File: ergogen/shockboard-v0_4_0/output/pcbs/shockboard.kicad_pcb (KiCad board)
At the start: 2 copper layers, 282.9 x 126 mm, 169 parts

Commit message: feat: added mounting holes
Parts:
- moved _8 12.2 mm to (316.2, 136.9)
- moved _7 12.2 mm to (108.6, 136.9)
- moved _3 11.1 mm to (97.5, 93.2)
- moved _4 11.1 mm to (327.3, 93.2)
- moved _1 11.1 mm to (173.7, 96.8)
- moved _2 11.1 mm to (251.0, 96.8)
- moved _6 10.6 mm to (258.8, 152.3)
- moved _5 10.6 mm to (165.9, 152.3)
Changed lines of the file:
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@@
     )
     (module "MountingHole_2.2mm_M2_Pad_Via" (version 20210722) (generator pcbnew) (layer "F.Cu")
-      (at 183.9168487 92.4964472 -8)
+      (at 173.7160154 96.8188307 -8)
       (fp_text reference "_1" (at 0 -3.2) (layer "F.SilkS") hide
         (effects (font (size 1 1) (thickness 0.15)))
@@
     )
     (module "MountingHole_2.2mm_M2_Pad_Via" (version 20210722) (generator pcbnew) (layer "F.Cu")
-      (at 240.83969309999998 92.4964472 8)
+      (at 251.04052639999998 96.8188307 8)
       (fp_text reference "_2" (at 0 -3.2) (layer "F.SilkS") hide
         (effects (font (size 1 1) (thickness 0.15)))
@@
     )
     (module "MountingHole_2.2mm_M2_Pad_Via" (version 20210722) (generator pcbnew) (layer "F.Cu")
-      (at 88.8671705 86.2068791 -8)
+      (at 97.4814305 93.1735516 -8)
       (fp_text reference "_3" (at 0 -3.2) (layer "F.SilkS") hide
         (effects (font (size 1 1) (thickness 0.15)))
@@
     )
     (module "MountingHole_2.2mm_M2_Pad_Via" (version 20210722) (generator pcbnew) (layer "F.Cu")
-      (at 335.8893713 86.2068791 8)
+      (at 327.2751113 93.1735516 8)
       (fp_text reference "_4" (at 0 -3.2) (layer "F.SilkS") hide
         (effects (font (size 1 1) (thickness 0.15)))
@@
     )
     (module "MountingHole_2.2mm_M2_Pad_Via" (version 20210722) (generator pcbnew) (layer "F.Cu")
-      (at 175.983982 148.9417271 -8)
+      (at 165.9153631 152.32335600000002 -8)
       (fp_text reference "_5" (at 0 -3.2) (layer "F.SilkS") hide
         (effects (font (size 1 1) (thickness 0.15)))
@@
     )
     (module "MountingHole_2.2mm_M2_Pad_Via" (version 20210722) (generator pcbnew) (layer "F.Cu")
-      (at 248.77255979999998 148.9417271 8)
+      (at 258.8411787 152.32335600000002 8)
       (fp_text reference "_6" (at 0 -3.2) (layer "F.SilkS") hide
         (effects (font (size 1 1) (thickness 0.15)))
@@
     )
     (module "MountingHole_2.2mm_M2_Pad_Via" (version 20210722) (generator pcbnew) (layer "F.Cu")
-      (at 99.7493971 145.296448 -8)
+      (at 108.5975789 136.9466169 -8)
       (fp_text reference "_7" (at 0 -3.2) (layer "F.SilkS") hide
         (effects (font (size 1 1) (thickness 0.15)))
@@
     )
     (module "MountingHole_2.2mm_M2_Pad_Via" (version 20210722) (generator pcbnew) (layer "F.Cu")
-      (at 325.00714469999997 145.296448 8)
+      (at 316.15896289999995 136.9466169 8)
       (fp_text reference "_8" (at 0 -3.2) (layer "F.SilkS") hide
         (effects (font (size 1 1) (thickness 0.15)))

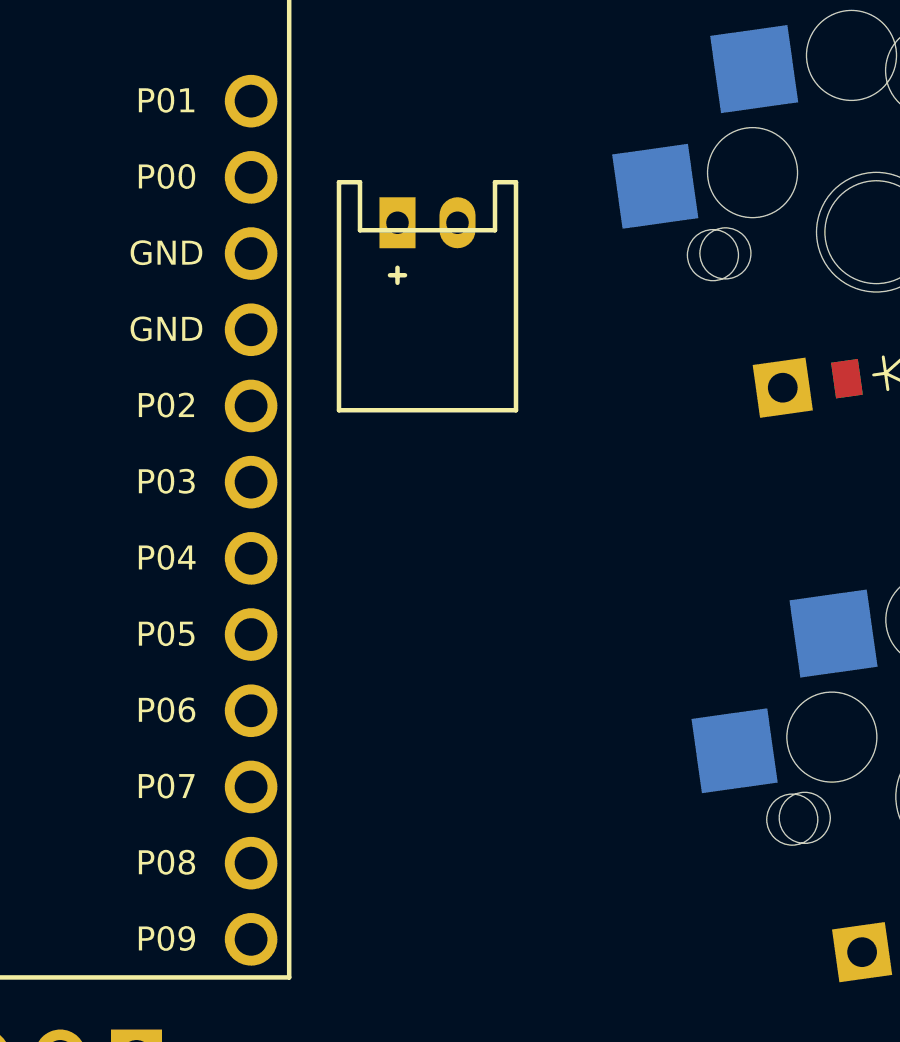
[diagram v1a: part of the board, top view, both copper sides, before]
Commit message: feat: move battery connector down
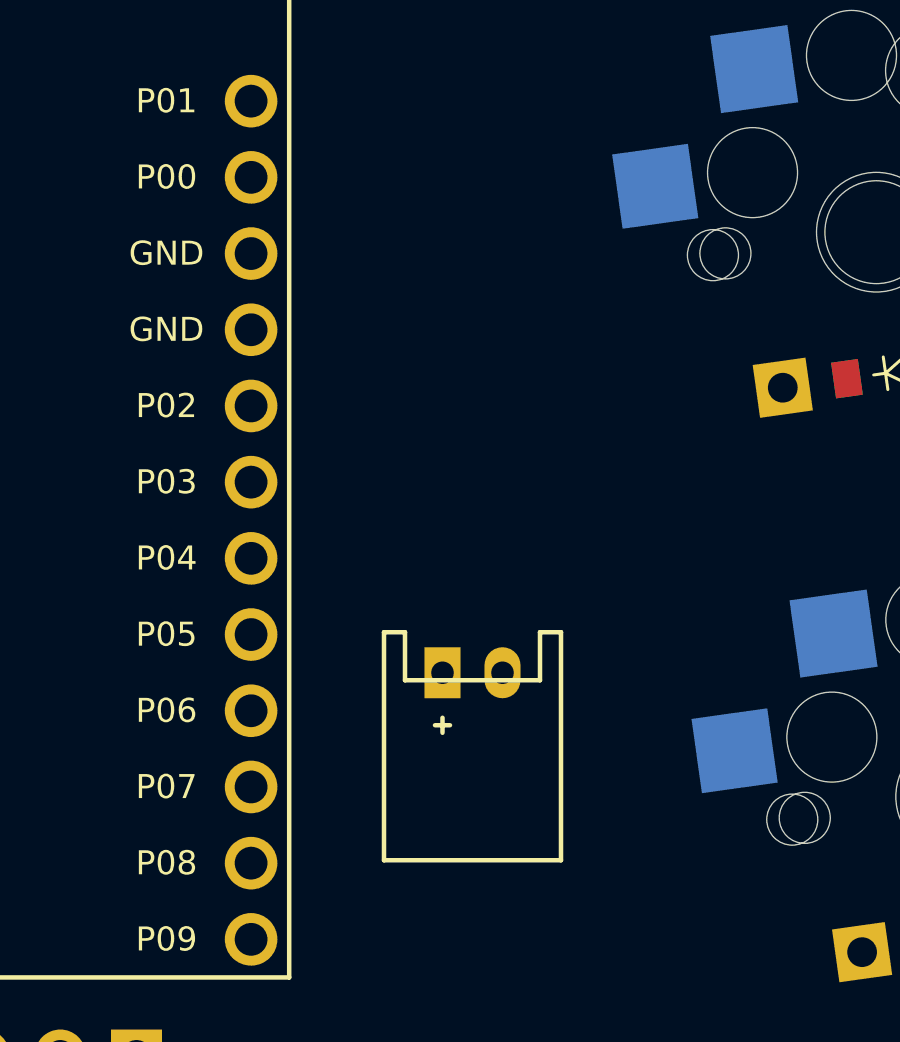
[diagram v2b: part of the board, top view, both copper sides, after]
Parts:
- moved JST1 15.1 mm to (227.4, 107.2)
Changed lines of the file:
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@@
         (descr "JST PH series connector, S2B-PH-K, side entry type, through hole, Datasheet: http://www.jst-mfg.com/product/pdf/eng/ePH.pdf")
         (tags "connector jst ph")
-        (at 225.87827089999996 92.1818495 0)
+        (at 227.37827089999996 107.1818495 0)
         (fp_text reference "JST1" (at 0 0) (layer F.SilkS) hide (effects (font (size 1.27 1.27) (thickness 0.15))))
         (fp_text value "" (at 0 0) (layer F.SilkS) hide (effects (font (size 1.27 1.27) (thickness 0.15))))

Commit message: feat: change and veryify pins
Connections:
- D1 pad 1: outer_home -> P20
- D1 pad 2: P7 -> outer_home
- D10 pad 1: ring_top -> P19
- D10 pad 2: P8 -> ring_top
- D11 pad 1: ring_num -> P18
- D11 pad 2: P9 -> ring_num
- D12 pad 1: middle_bottom -> P21
- D12 pad 2: P6 -> middle_bottom
- D13 pad 1: middle_home -> P20
- D13 pad 2: P7 -> middle_home
- D14 pad 1: middle_top -> P19
- D14 pad 2: P8 -> middle_top
- D15 pad 1: middle_num -> P18
- D15 pad 2: P9 -> middle_num
- D16 pad 1: index_bottom -> P21
- D16 pad 2: P6 -> index_bottom
- D17 pad 1: index_home -> P20
- D17 pad 2: P7 -> index_home
- D18 pad 1: index_top -> P19
- D18 pad 2: P8 -> index_top
- D19 pad 1: index_num -> P18
- D19 pad 2: P9 -> index_num
- D2 pad 1: outer_top -> P19
- D2 pad 2: P8 -> outer_top
- D20 pad 1: inner_bottom -> P21
- D20 pad 2: P6 -> inner_bottom
- D21 pad 1: inner_home -> P20
- D21 pad 2: P7 -> inner_home
- D22 pad 1: inner_top -> P19
- D22 pad 2: P8 -> inner_top
- D23 pad 1: inner_num -> P18
- D23 pad 2: P9 -> inner_num
- D24 pad 1: outer_thumb -> P15
- D24 pad 2: P16 -> outer_thumb
- D25 pad 1: middle_thumb -> P15
- D25 pad 2: P16 -> middle_thumb
- D26 pad 1: inner_thumb -> P15
- D26 pad 2: P16 -> inner_thumb
- D27 pad 1: mirror_outer_home -> P0
- D27 pad 2: P7 -> mirror_outer_home
- D28 pad 1: mirror_outer_top -> P4
- D28 pad 2: P8 -> mirror_outer_top
- D29 pad 1: mirror_outer_num -> P5
- D29 pad 2: P9 -> mirror_outer_num
- D3 pad 1: outer_num -> P18
- D3 pad 2: P9 -> outer_num
- D30 pad 1: mirror_pinky_bottom -> P1
- D30 pad 2: P6 -> mirror_pinky_bottom
- D31 pad 1: mirror_pinky_home -> P0
- D31 pad 2: P7 -> mirror_pinky_home
- D32 pad 1: mirror_pinky_top -> P4
- D32 pad 2: P8 -> mirror_pinky_top
- D33 pad 1: mirror_pinky_num -> P5
- D33 pad 2: P9 -> mirror_pinky_num
- D34 pad 1: mirror_ring_bottom -> P1
- D34 pad 2: P6 -> mirror_ring_bottom
- D35 pad 1: mirror_ring_home -> P0
- D35 pad 2: P7 -> mirror_ring_home
- D36 pad 1: mirror_ring_top -> P4
- D36 pad 2: P8 -> mirror_ring_top
- D37 pad 1: mirror_ring_num -> P5
- D37 pad 2: P9 -> mirror_ring_num
- D38 pad 1: mirror_middle_bottom -> P1
- D38 pad 2: P6 -> mirror_middle_bottom
- D39 pad 1: mirror_middle_home -> P0
- D39 pad 2: P7 -> mirror_middle_home
- D4 pad 1: pinky_bottom -> P21
- D4 pad 2: P6 -> pinky_bottom
- D40 pad 1: mirror_middle_top -> P4
- D40 pad 2: P8 -> mirror_middle_top
- D41 pad 1: mirror_middle_num -> P5
- D41 pad 2: P9 -> mirror_middle_num
- D42 pad 1: mirror_index_bottom -> P1
- D42 pad 2: P6 -> mirror_index_bottom
- D43 pad 1: mirror_index_home -> P0
- D43 pad 2: P7 -> mirror_index_home
- D44 pad 1: mirror_index_top -> P4
- D44 pad 2: P8 -> mirror_index_top
- D45 pad 1: mirror_index_num -> P5
- D45 pad 2: P9 -> mirror_index_num
- D46 pad 1: mirror_inner_bottom -> P1
- D46 pad 2: P6 -> mirror_inner_bottom
- D47 pad 1: mirror_inner_home -> P0
- D47 pad 2: P7 -> mirror_inner_home
- D48 pad 1: mirror_inner_top -> P4
- D48 pad 2: P8 -> mirror_inner_top
- D49 pad 1: mirror_inner_num -> P5
- D49 pad 2: P9 -> mirror_inner_num
- D5 pad 1: pinky_home -> P20
- D5 pad 2: P7 -> pinky_home
- D50 pad 1: mirror_outer_thumb -> P6
- D50 pad 2: P16 -> mirror_outer_thumb
- D51 pad 1: mirror_middle_thumb -> P6
- D51 pad 2: P16 -> mirror_middle_thumb
- D52 pad 1: mirror_inner_thumb -> P6
- D52 pad 2: P16 -> mirror_inner_thumb
- D6 pad 1: pinky_top -> P19
- D6 pad 2: P8 -> pinky_top
- D7 pad 1: pinky_num -> P18
- D7 pad 2: P9 -> pinky_num
- D8 pad 1: ring_bottom -> P21
- D8 pad 2: P6 -> ring_bottom
- D9 pad 1: ring_home -> P20
- D9 pad 2: P7 -> ring_home
- S1 pad 1: outer_home -> P14
- S1 pad 2: P21 -> outer_home
- S10 pad 1: ring_top -> P10
- S10 pad 2: P19 -> ring_top
- S100 pad 1: mirror_inner_top -> P9
- S100 pad 2: P5 -> mirror_inner_top
- S101 pad 1: mirror_inner_num -> P9
- S101 pad 2: P5 -> mirror_inner_num
- S102 pad 1: mirror_outer_thumb -> P7
- S102 pad 2: P3 -> mirror_outer_thumb
- S103 pad 1: mirror_middle_thumb -> P8
- S103 pad 2: P4 -> mirror_middle_thumb
- S104 pad 1: mirror_inner_thumb -> P9
- S104 pad 2: P5 -> mirror_inner_thumb
- S11 pad 1: ring_num -> P10
- S11 pad 2: P19 -> ring_num
- S12 pad 1: middle_bottom -> P7
- S12 pad 2: P18 -> middle_bottom
- S13 pad 1: middle_home -> P7
- S13 pad 2: P18 -> middle_home
- S14 pad 1: middle_top -> P7
- S14 pad 2: P18 -> middle_top
- S15 pad 1: middle_num -> P7
- S15 pad 2: P18 -> middle_num
- S16 pad 1: index_bottom -> P8
- S16 pad 2: P15 -> index_bottom
- S17 pad 1: index_home -> P8
- S17 pad 2: P15 -> index_home
- S18 pad 1: index_top -> P8
- S18 pad 2: P15 -> index_top
- S19 pad 1: index_num -> P8
- S19 pad 2: P15 -> index_num
- S2 pad 1: outer_top -> P14
- S2 pad 2: P21 -> outer_top
- S20 pad 1: inner_bottom -> P9
- S20 pad 2: P14 -> inner_bottom
- S21 pad 1: inner_home -> P9
- S21 pad 2: P14 -> inner_home
- S22 pad 1: inner_top -> P9
- S22 pad 2: P14 -> inner_top
- S23 pad 1: inner_num -> P9
- S23 pad 2: P14 -> inner_num
- S24 pad 1: outer_thumb -> P7
- S24 pad 2: P18 -> outer_thumb
- S25 pad 1: middle_thumb -> P8
- S25 pad 2: P15 -> middle_thumb
- S26 pad 1: inner_thumb -> P9
- S26 pad 2: P14 -> inner_thumb
- S27 pad 1: mirror_outer_home -> P14
- S27 pad 2: P1 -> mirror_outer_home
- S28 pad 1: mirror_outer_top -> P14
- S28 pad 2: P1 -> mirror_outer_top
- S29 pad 1: mirror_outer_num -> P14
- S29 pad 2: P1 -> mirror_outer_num
- S3 pad 1: outer_num -> P14
- S3 pad 2: P21 -> outer_num
- S30 pad 1: mirror_pinky_bottom -> P16
- S30 pad 2: P0 -> mirror_pinky_bottom
- S31 pad 1: mirror_pinky_home -> P16
- S31 pad 2: P0 -> mirror_pinky_home
- S32 pad 1: mirror_pinky_top -> P16
- S32 pad 2: P0 -> mirror_pinky_top
- S33 pad 1: mirror_pinky_num -> P16
- S33 pad 2: P0 -> mirror_pinky_num
- S34 pad 1: mirror_ring_bottom -> P10
- S34 pad 2: P2 -> mirror_ring_bottom
- S35 pad 1: mirror_ring_home -> P10
- S35 pad 2: P2 -> mirror_ring_home
- S36 pad 1: mirror_ring_top -> P10
- S36 pad 2: P2 -> mirror_ring_top
- S37 pad 1: mirror_ring_num -> P10
- S37 pad 2: P2 -> mirror_ring_num
- S38 pad 1: mirror_middle_bottom -> P7
- S38 pad 2: P3 -> mirror_middle_bottom
- S39 pad 1: mirror_middle_home -> P7
- S39 pad 2: P3 -> mirror_middle_home
- S4 pad 1: pinky_bottom -> P16
- S4 pad 2: P20 -> pinky_bottom
- S40 pad 1: mirror_middle_top -> P7
- S40 pad 2: P3 -> mirror_middle_top
- S41 pad 1: mirror_middle_num -> P7
- S41 pad 2: P3 -> mirror_middle_num
- S42 pad 1: mirror_index_bottom -> P8
- S42 pad 2: P4 -> mirror_index_bottom
- S43 pad 1: mirror_index_home -> P8
- S43 pad 2: P4 -> mirror_index_home
- S44 pad 1: mirror_index_top -> P8
- S44 pad 2: P4 -> mirror_index_top
- S45 pad 1: mirror_index_num -> P8
- S45 pad 2: P4 -> mirror_index_num
- S46 pad 1: mirror_inner_bottom -> P9
- S46 pad 2: P5 -> mirror_inner_bottom
- S47 pad 1: mirror_inner_home -> P9
- S47 pad 2: P5 -> mirror_inner_home
- S48 pad 1: mirror_inner_top -> P9
- S48 pad 2: P5 -> mirror_inner_top
- S49 pad 1: mirror_inner_num -> P9
- S49 pad 2: P5 -> mirror_inner_num
- S5 pad 1: pinky_home -> P16
- S5 pad 2: P20 -> pinky_home
- S50 pad 1: mirror_outer_thumb -> P7
- S50 pad 2: P3 -> mirror_outer_thumb
- S51 pad 1: mirror_middle_thumb -> P8
- S51 pad 2: P4 -> mirror_middle_thumb
- S52 pad 1: mirror_inner_thumb -> P9
- S52 pad 2: P5 -> mirror_inner_thumb
- S53 pad 1: outer_home -> P14
- S53 pad 2: P21 -> outer_home
- S54 pad 1: outer_top -> P14
- S54 pad 2: P21 -> outer_top
- S55 pad 1: outer_num -> P14
- S55 pad 2: P21 -> outer_num
- S56 pad 1: pinky_bottom -> P16
- S56 pad 2: P20 -> pinky_bottom
- S57 pad 1: pinky_home -> P16
- S57 pad 2: P20 -> pinky_home
- S58 pad 1: pinky_top -> P16
- S58 pad 2: P20 -> pinky_top
- S59 pad 1: pinky_num -> P16
- S59 pad 2: P20 -> pinky_num
- S6 pad 1: pinky_top -> P16
- S6 pad 2: P20 -> pinky_top
- S60 pad 1: ring_bottom -> P10
- S60 pad 2: P19 -> ring_bottom
- S61 pad 1: ring_home -> P10
- S61 pad 2: P19 -> ring_home
- S62 pad 1: ring_top -> P10
- S62 pad 2: P19 -> ring_top
- S63 pad 1: ring_num -> P10
- S63 pad 2: P19 -> ring_num
- S64 pad 1: middle_bottom -> P7
- S64 pad 2: P18 -> middle_bottom
- S65 pad 1: middle_home -> P7
- S65 pad 2: P18 -> middle_home
- S66 pad 1: middle_top -> P7
- S66 pad 2: P18 -> middle_top
- S67 pad 1: middle_num -> P7
- S67 pad 2: P18 -> middle_num
- S68 pad 1: index_bottom -> P8
- S68 pad 2: P15 -> index_bottom
- S69 pad 1: index_home -> P8
- S69 pad 2: P15 -> index_home
- S7 pad 1: pinky_num -> P16
- S7 pad 2: P20 -> pinky_num
- S70 pad 1: index_top -> P8
- S70 pad 2: P15 -> index_top
- S71 pad 1: index_num -> P8
- S71 pad 2: P15 -> index_num
- S72 pad 1: inner_bottom -> P9
- S72 pad 2: P14 -> inner_bottom
- S73 pad 1: inner_home -> P9
- S73 pad 2: P14 -> inner_home
- S74 pad 1: inner_top -> P9
- S74 pad 2: P14 -> inner_top
- S75 pad 1: inner_num -> P9
- S75 pad 2: P14 -> inner_num
- S76 pad 1: outer_thumb -> P7
- S76 pad 2: P18 -> outer_thumb
- S77 pad 1: middle_thumb -> P8
- S77 pad 2: P15 -> middle_thumb
- S78 pad 1: inner_thumb -> P9
- S78 pad 2: P14 -> inner_thumb
- S79 pad 1: mirror_outer_home -> P14
- S79 pad 2: P1 -> mirror_outer_home
- S8 pad 1: ring_bottom -> P10
- S8 pad 2: P19 -> ring_bottom
- S80 pad 1: mirror_outer_top -> P14
- S80 pad 2: P1 -> mirror_outer_top
- S81 pad 1: mirror_outer_num -> P14
- S81 pad 2: P1 -> mirror_outer_num
- S82 pad 1: mirror_pinky_bottom -> P16
- S82 pad 2: P0 -> mirror_pinky_bottom
- S83 pad 1: mirror_pinky_home -> P16
- S83 pad 2: P0 -> mirror_pinky_home
- S84 pad 1: mirror_pinky_top -> P16
- S84 pad 2: P0 -> mirror_pinky_top
- S85 pad 1: mirror_pinky_num -> P16
- S85 pad 2: P0 -> mirror_pinky_num
- S86 pad 1: mirror_ring_bottom -> P10
- S86 pad 2: P2 -> mirror_ring_bottom
- S87 pad 1: mirror_ring_home -> P10
- S87 pad 2: P2 -> mirror_ring_home
- S88 pad 1: mirror_ring_top -> P10
- S88 pad 2: P2 -> mirror_ring_top
- S89 pad 1: mirror_ring_num -> P10
- S89 pad 2: P2 -> mirror_ring_num
- S9 pad 1: ring_home -> P10
- S9 pad 2: P19 -> ring_home
- S90 pad 1: mirror_middle_bottom -> P7
- S90 pad 2: P3 -> mirror_middle_bottom
- S91 pad 1: mirror_middle_home -> P7
- S91 pad 2: P3 -> mirror_middle_home
- S92 pad 1: mirror_middle_top -> P7
- S92 pad 2: P3 -> mirror_middle_top
- S93 pad 1: mirror_middle_num -> P7
- S93 pad 2: P3 -> mirror_middle_num
- S94 pad 1: mirror_index_bottom -> P8
- S94 pad 2: P4 -> mirror_index_bottom
- S95 pad 1: mirror_index_home -> P8
- S95 pad 2: P4 -> mirror_index_home
- S96 pad 1: mirror_index_top -> P8
- S96 pad 2: P4 -> mirror_index_top
- S97 pad 1: mirror_index_num -> P8
- S97 pad 2: P4 -> mirror_index_num
- S98 pad 1: mirror_inner_bottom -> P9
- S98 pad 2: P5 -> mirror_inner_bottom
- S99 pad 1: mirror_inner_home -> P9
- S99 pad 2: P5 -> mirror_inner_home

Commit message: feat: complete board with fab, no silkscreen yet
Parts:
- removed B1: , E73:SW_TACT_ALPS_SKQGABE010
- added RST1: reset_switch_tht_top, ceoloide:reset_switch_tht_top, F.Cu at (198.9, 92.2)
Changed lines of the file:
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@@
         (net 70 "GND"))
         )
-    (module E73:SW_TACT_ALPS_SKQGABE010 (layer F.Cu)
-        (descr "Low-profile SMD Tactile Switch, https://www.e-switch.com/product-catalog/tact/product-lines/tl3342-series-low-profile-smt-tact-switch")
-        (tags "SPST Tactile Switch")
-        (at 198.87827089999996 92.1818495 90)
-        (fp_text reference "B1" (at 0 0) (layer F.SilkS) hide (effects (font (size 1.27 1.27) (thickness 0.15))))
-        (fp_text value "" (at 0 0) (layer F.SilkS) hide (effects (font (size 1.27 1.27) (thickness 0.15))))
-        (fp_line (start 2.75 1.25) (end 1.25 2.75) (layer F.SilkS) (width 0.15))
-        (fp_line (start 2.75 -1.25) (end 1.25 -2.75) (layer F.SilkS) (width 0.15))
-        (fp_line (start 2.75 -1.25) (end 2.75 1.25) (layer F.SilkS) (width 0.15))
-        (fp_line (start -1.25 2.75) (end 1.25 2.75) (layer F.SilkS) (width 0.15))
-        (fp_line (start -1.25 -2.75) (end 1.25 -2.75) (layer F.SilkS) (width 0.15))
-        (fp_line (start -2.75 1.25) (end -1.25 2.75) (layer F.SilkS) (width 0.15))
-        (fp_line (start -2.75 -1.25) (end -1.25 -2.75) (layer F.SilkS) (width 0.15))
-        (fp_line (start -2.75 -1.25) (end -2.75 1.25) (layer F.SilkS) (width 0.15))
-        (pad 1 smd rect (at -3.1 -1.85 90) (size 1.8 1.1) (layers F.Cu F.Paste F.Mask) (net 70 "GND"))
-        (pad 1 smd rect (at 3.1 -1.85 90) (size 1.8 1.1) (layers F.Cu F.Paste F.Mask) (net 70 "GND"))
-        (pad 2 smd rect (at -3.1 1.85 90) (size 1.8 1.1) (layers F.Cu F.Paste F.Mask) (net 71 "RST"))
-        (pad 2 smd rect (at 3.1 1.85 90) (size 1.8 1.1) (layers F.Cu F.Paste F.Mask) (net 71 "RST"))
-    )
+            (module "ceoloide:reset_switch_tht_top" (layer F.Cu)
+                (at 198.87827089999996 92.1818495 90)
+                (fp_text value "reset_switch_tht_top" (at 0 -2.55 180) (layer F.Fab) (effects (font (size 1 1) (thickness 0.15))))
+                (fp_text reference "RST1" (at 0 2.55 180) (layer F.SilkS) hide (effects (font (size 1 1) (thickness 0.15))))
+                (fp_text user "RST" (at 0 0 90) (layer F.SilkS) (effects (font (size 1 1) (thickness 0.15))))
+                (fp_line (start -3 1.75) (end 3 1.75) (layer F.SilkS) (width 0.15))
+                (fp_line (start 3 1.75) (end 3 1.5) (layer F.SilkS) (width 0.15))
+                (fp_line (start -3 1.75) (end -3 1.5) (layer F.SilkS) (width 0.15))
+                (fp_line (start -3 -1.75) (end -3 -1.5) (layer F.SilkS) (width 0.15))
+                (fp_line (start -3 -1.75) (end 3 -1.75) (layer F.SilkS) (width 0.15))
+                (fp_line (start 3 -1.75) (end 3 -1.5) (layer F.SilkS) (width 0.15))
+                (pad 2 thru_hole circle (at -3.25 0 90) (size 2 2) (drill 1.3) (layers *.Cu *.Mask) (net 70 "GND"))
+                (pad 1 thru_hole circle (at 3.25 0 90) (size 2 2) (drill 1.3) (layers *.Cu *.Mask) (net 71 "RST"))
+            )
         (module E73:SPDT_C128955 (layer F.Cu)
             (at 319.5512817 72.3458067 -7.5)
